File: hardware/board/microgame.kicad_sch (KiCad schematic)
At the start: 24 parts, among them U1 ATTINY85-20SU

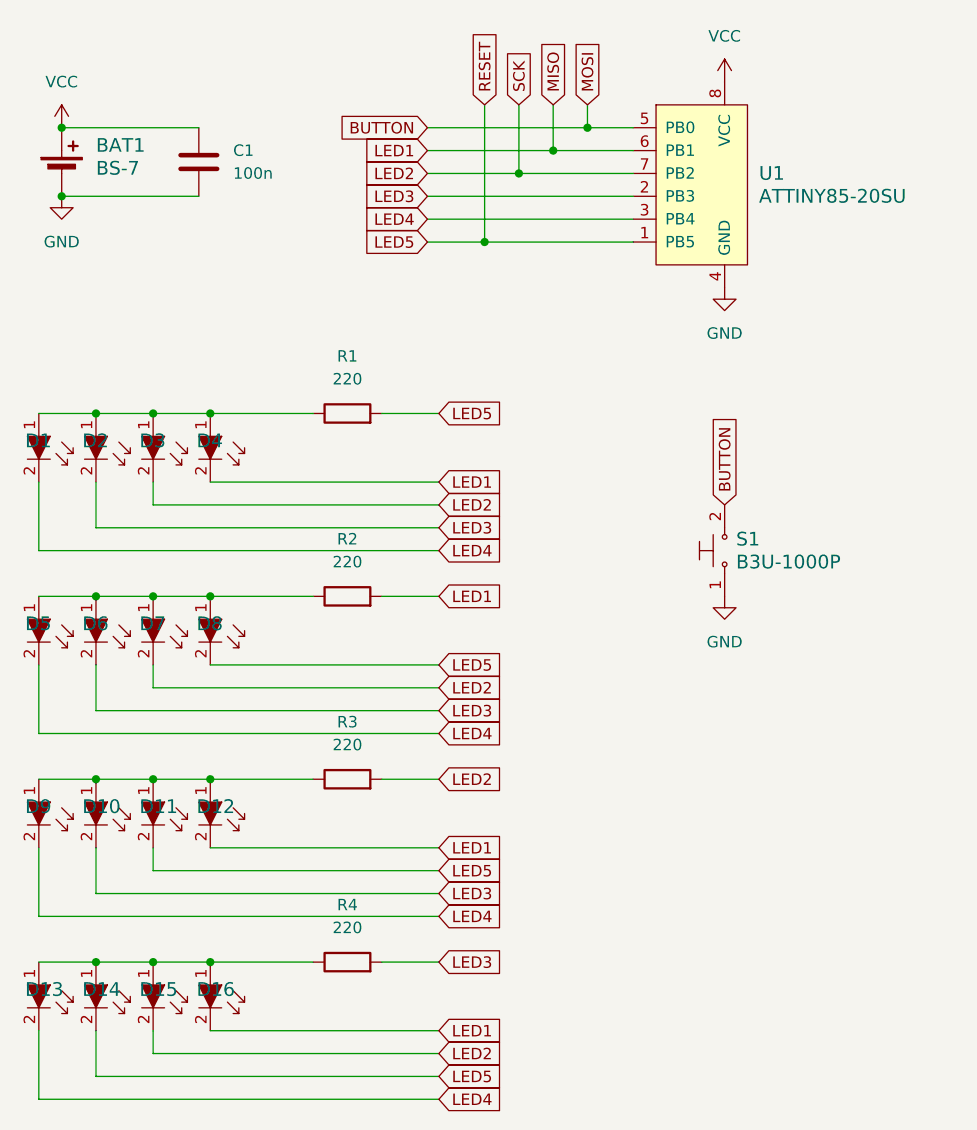
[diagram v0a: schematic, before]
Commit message: Updated design to have a sane pin mapping. Added initial simulator program and firmware.
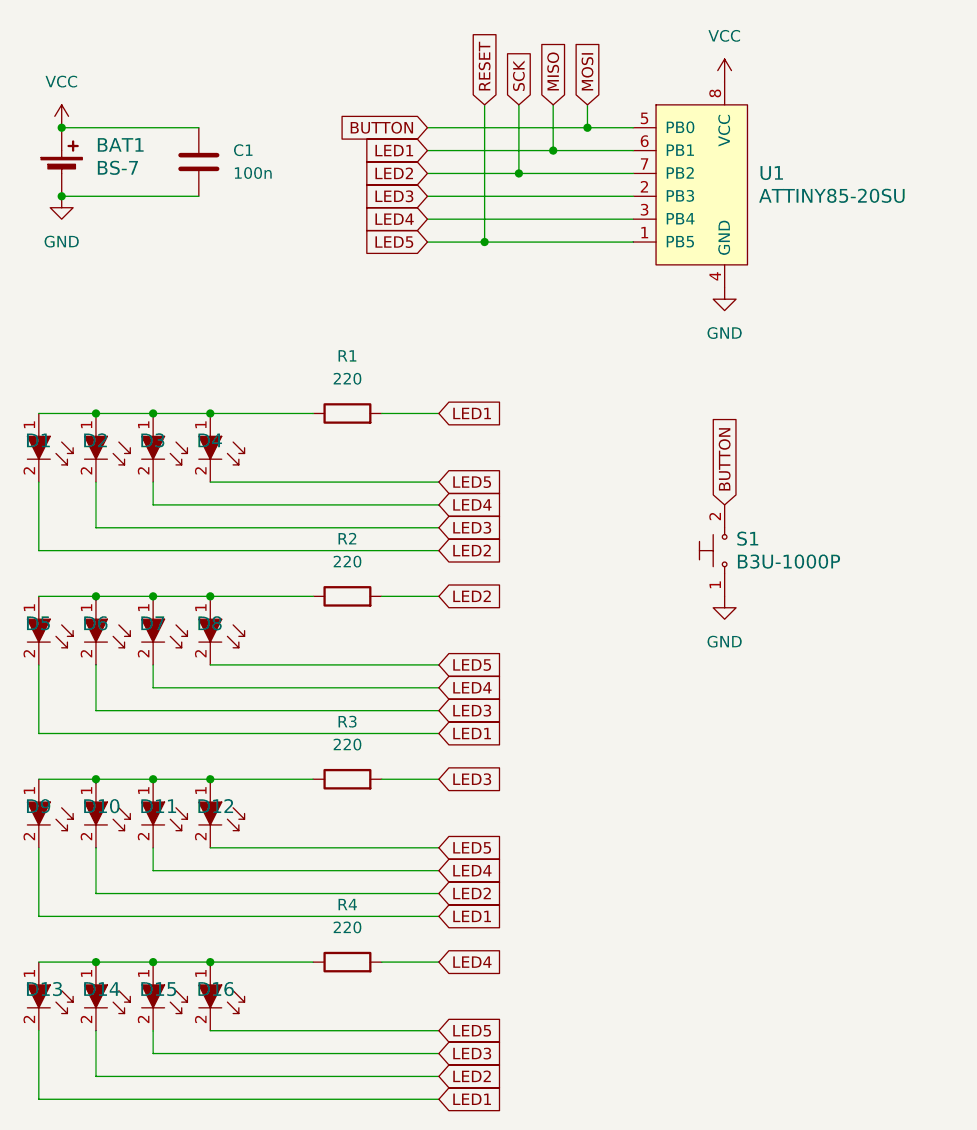
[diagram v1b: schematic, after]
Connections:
- net LED1: now also D13.2, D5.2, D9.2, R1.2; no longer D12.2, D16.2, D4.2, R2.2
- net LED2: now also D1.2, D10.2, D14.2, R2.2; no longer D15.2, D3.2, D7.2, R3.2
- net LED3: now also D15.2, R3.2; no longer D10.2, R4.2
- net LED4: now also D11.2, D3.2, D7.2, R4.2; no longer D1.2, D13.2, D5.2, D9.2
- net LED5: now also D12.2, D16.2, D4.2; no longer D11.2, D14.2, R1.2

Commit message: Updated BOM
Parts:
- BAT1: value BS-7 -> Keystone 3034
- U1: value ATTINY85-20SU -> ATTINY25-20SSU
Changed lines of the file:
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@@
 			)
 		)
-		(property "Value" "BS-7"
+		(property "Value" "Keystone 3034"
 			(at 31.75 34.9884 0)
 			(effects
@@
 		(on_board yes)
 		(dnp no)
-		(fields_autoplaced yes)
 		(property "Reference" "U1"
 			(at 105.41 35.5599 0)
@@
 			)
 		)
-		(property "Value" "ATTINY85-20SU"
+		(property "Value" "ATTINY25-20SSU"
 			(at 105.41 38.0999 0)
 			(effects
